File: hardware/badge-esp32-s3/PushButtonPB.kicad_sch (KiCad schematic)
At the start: 2 parts, among them SW1 TS665CJ

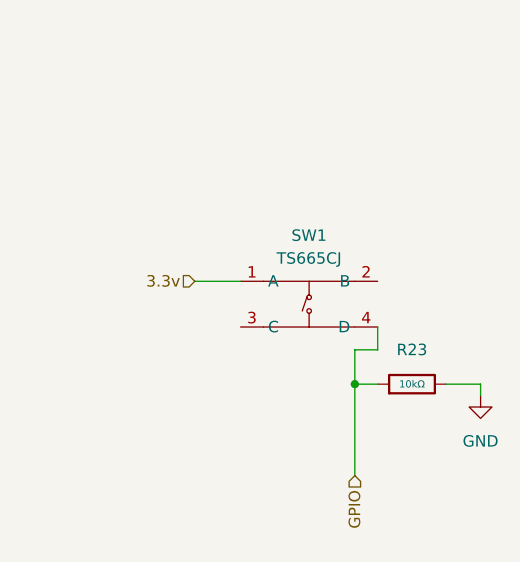
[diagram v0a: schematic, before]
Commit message: Fixed Button, Added Joystick
Button's extra resistor was removed
Buttons were added to Onboard Peripheral sub sheet (all 6)
Joystick was added to library + onboard Peripheral sub sheet in its own sub sheet.
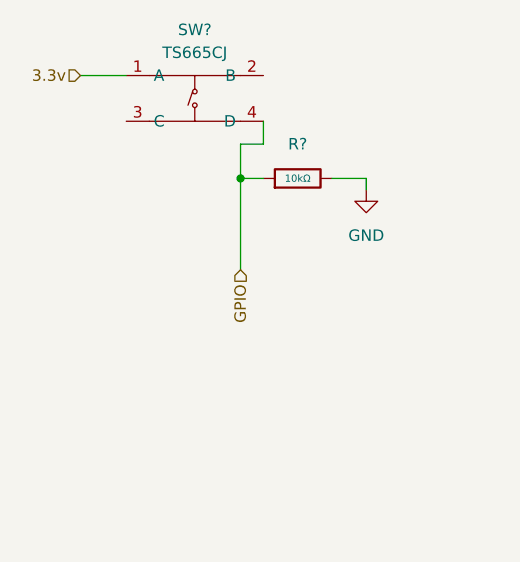
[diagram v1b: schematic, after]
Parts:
- renumbered R23 to R?, SW1 to SW?
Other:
- moved on the sheet: R?, SW?
